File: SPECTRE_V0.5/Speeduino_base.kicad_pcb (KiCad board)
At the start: 2 copper layers, 100 x 93 mm, 213 parts, among them J1 Conn_01x06_Male, J2 Conn_02x04_Odd_Even, Q1 AO3400, Q10 AO3401A, Q11 AO3401A, Q12 BSP78, Q13 BSP78, Q14 BSP78, Q15 BSP78, Q16 AO3422, Q17 AO3422, Q18 BSP78, Q19 BSP78, Q2 AO3400, Q20 BSP78, Q21 AO3401A, Q22 AO3401A, Q23 BSP78, Q24 BSP78, Q25 BSP78, Q26 BSP78, Q3 AO3400, Q4 AO3400, Q5 AO3400, Q6 AO3400, Q7 AO3400, Q8 AO3422, Q9 AO3422, U1 MAX9926UAEE+, U2 LM78M05_TO220, U3 TL431DBZ, U4 molex_48pin, U5 TJA1050, U6 MAX3232

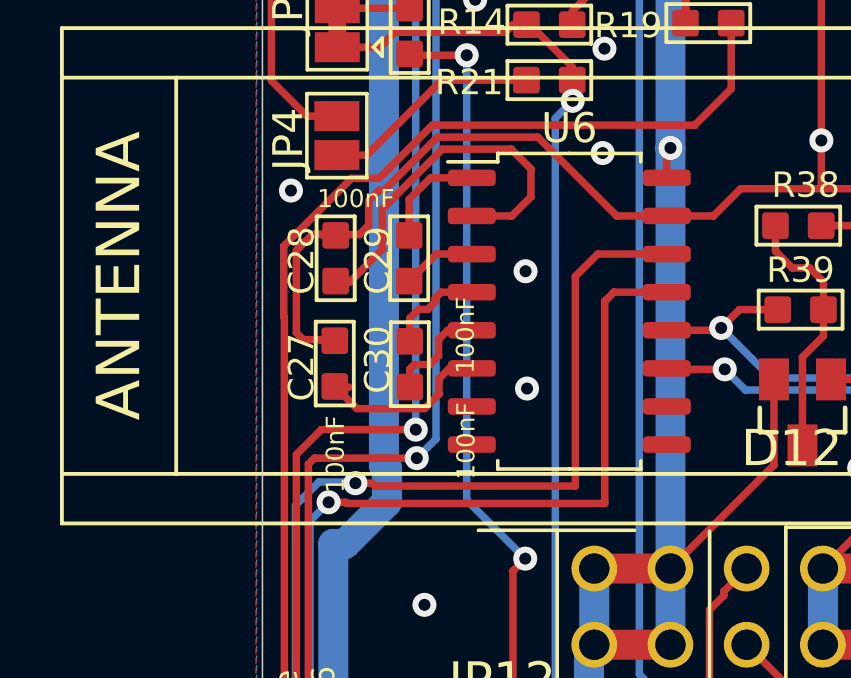
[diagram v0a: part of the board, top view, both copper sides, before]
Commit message: Removed peak&hold driver from this repo. Update resistor values in schematic to values that work. Cleaned up resistor naming.
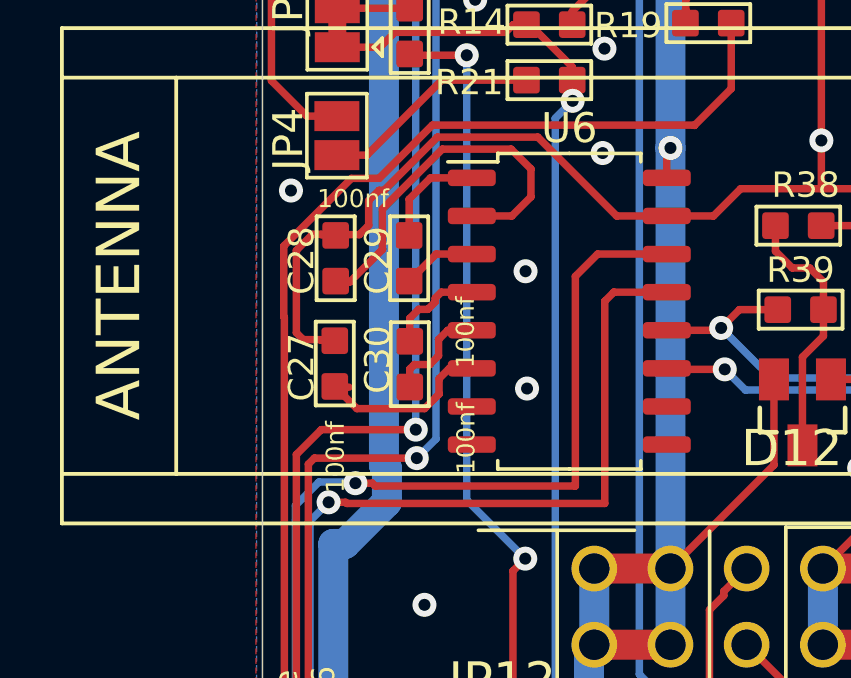
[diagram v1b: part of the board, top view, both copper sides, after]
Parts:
- C27, C28, C29, C30: value 100nF -> 100nf
- R10, R26, R29, R47: value 9.1k -> 9k1
- R25: value 4.7k -> 4K7
- R28, R46, R9: value 4.7k -> 4k7
- R34, R41, R52, R55, R61, R65, R84, R85, R88: value 100 -> 100R
- R44: value 8k3 -> 33k
- R45: value 1k2 -> 5k1
- R66: value 100k -> 10k
- R67: value 1k -> 100R
- R70: value 180 -> 220R
- R71: value 82 -> 100R
- R72: value 560 -> 470R
- R75: value 120 -> 120R
- R78, R79, R96, R97: value 470 -> 470R

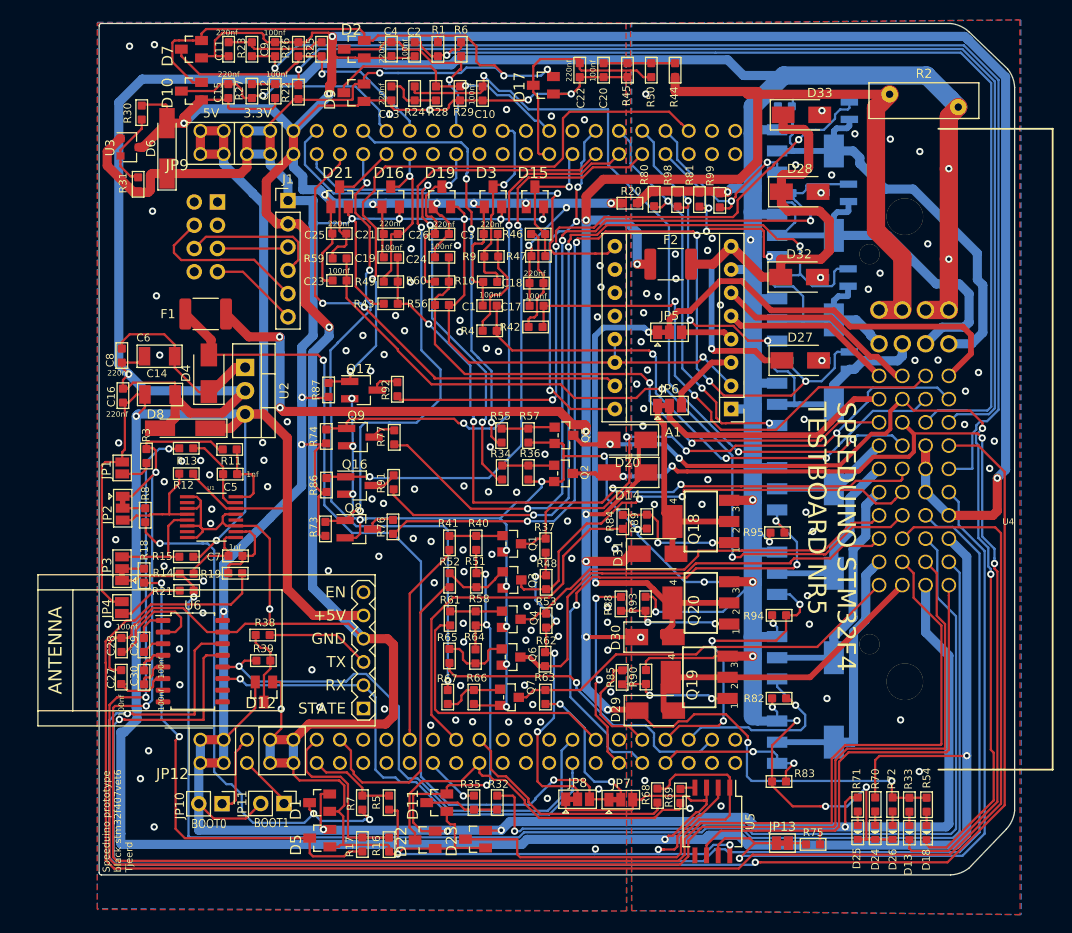
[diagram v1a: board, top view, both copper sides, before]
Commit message: clean-up board V0.5 started on board V0.5.1
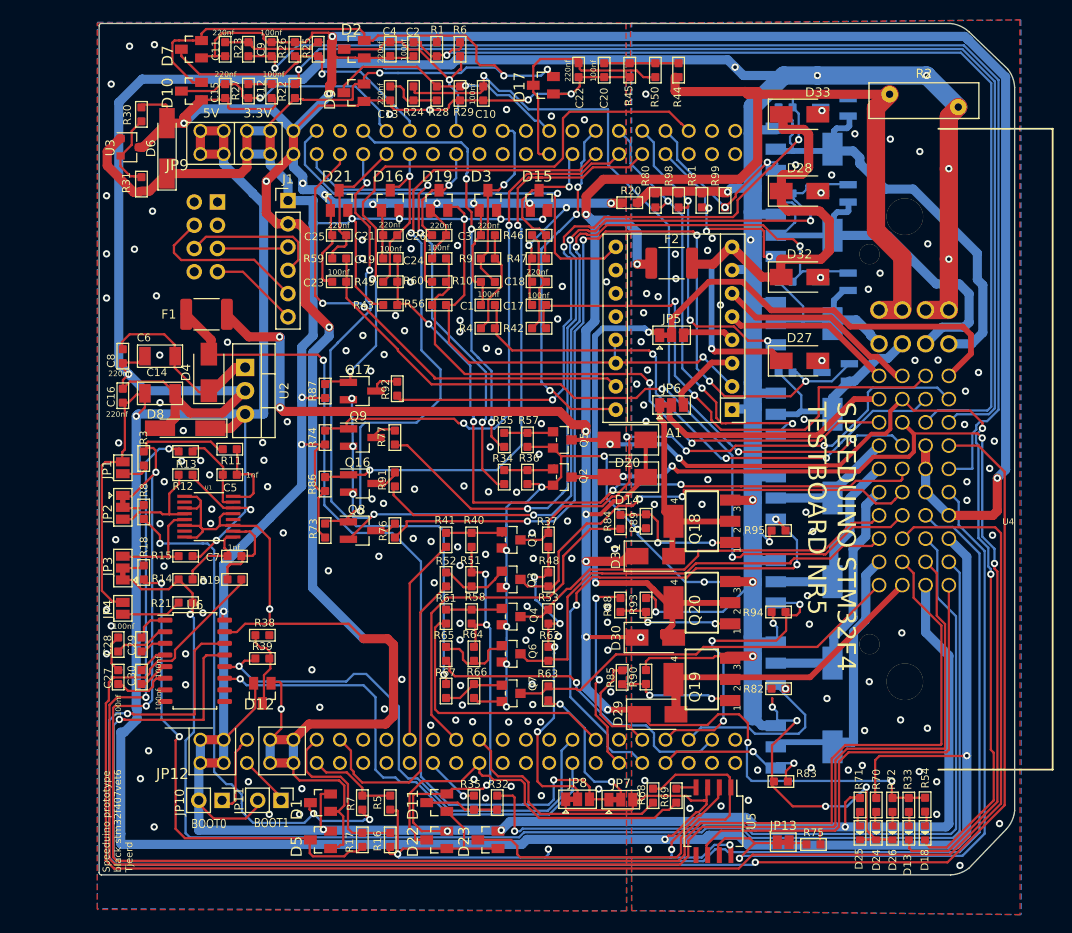
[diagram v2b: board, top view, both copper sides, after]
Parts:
- removed U$1: WIRELESS-BLUETOOTH-HC-05, Speeduino_base:WIRELESS-BLUETOOTH-HC-05
- moved D23 1.36 mm to (156.5, 106.2)
- moved R78 1.34 mm to (189.0, 55.1)
- moved R21 1.32 mm to (123.4, 80.3)
- moved Q10 1.29 mm to (194.4, 55.1)
- moved D22 1.27 mm to (150.9, 106.2)
- moved Q12 1.10 mm to (191.0, 59.7)
- moved R82 1.05 mm to (188.2, 89.7)
- moved Q24 1.02 mm to (191.0, 68.8)
- moved Q23 0.94 mm to (191.0, 78.0)
- moved R97 0.91 mm to (189.0, 45.2)
- moved R37 0.70 mm to (163.1, 73.4)
- moved R62 0.69 mm to (163.1, 85.9)
- moved D3 0.68 mm to (156.5, 36.3)
- moved R67 0.68 mm to (151.9, 89.9)
- moved R19 0.68 mm to (128.8, 77.7)
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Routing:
- net 5V: track 366.8 -> 331.9 mm, vias 4 -> 5
- net GND: track 631.2 -> 612.0 mm, vias 114 -> 141
- net /BT_TX: track 11.5 -> 0.00 mm
- net Net-(C28-Pad1): track 12.6 -> 6.03 mm
- net Net-(Q22-Pad1): track 83.0 -> 78.2 mm
- net PE9: track 44.6 -> 48.5 mm
- net VR2-: track 185.4 -> 181.9 mm
- net INJ6-OUT: track 25.1 -> 21.7 mm
- net Net-(Q10-Pad1): track 102.7 -> 99.4 mm
- net 3.3V: track 508.0 -> 504.8 mm
- net Net-(Q21-Pad1): track 88.4 -> 86.1 mm
- net VBAT_F1: track 96.1 -> 98.1 mm
- net PE13: track 21.8 -> 20.0 mm
- net BARO: track 57.8 -> 59.7 mm
- net PWR_GND: track 488.4 -> 490.2 mm, vias 71 -> 91
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
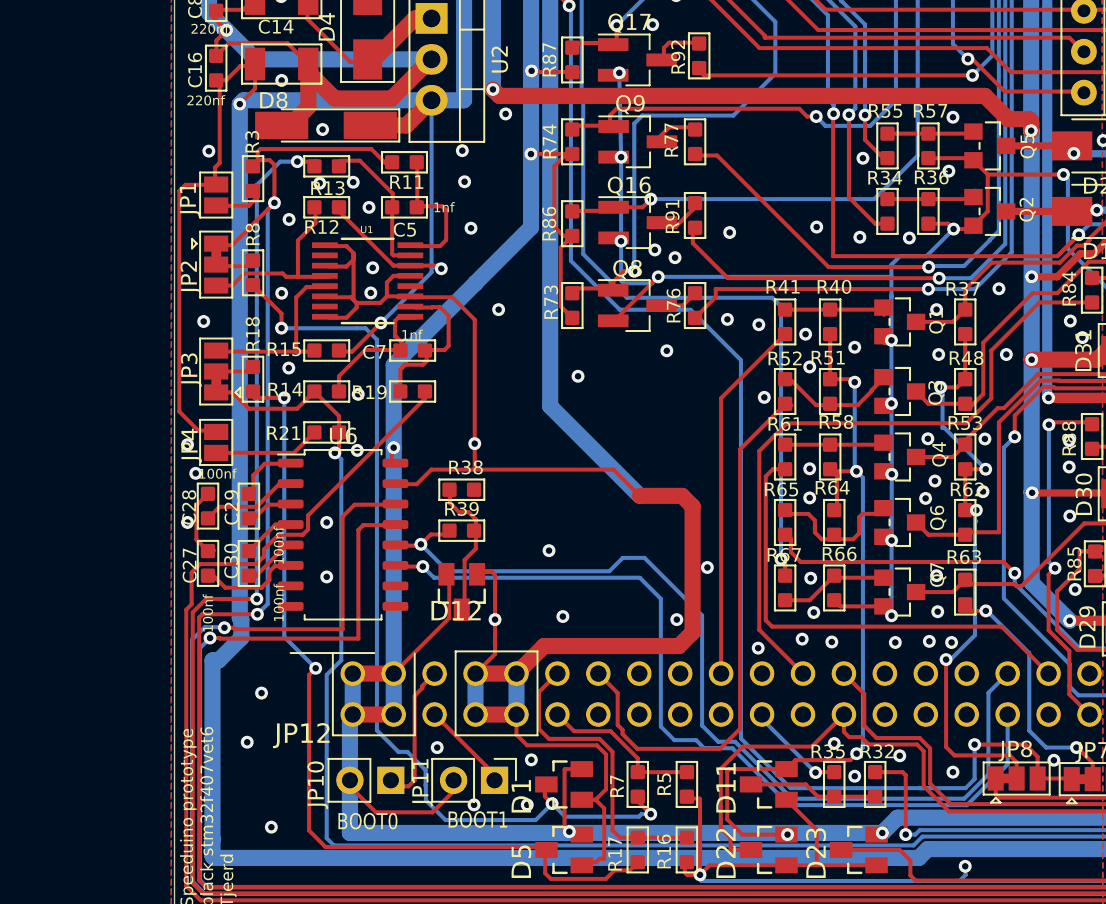
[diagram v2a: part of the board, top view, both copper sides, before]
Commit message: re-add bluetooth module
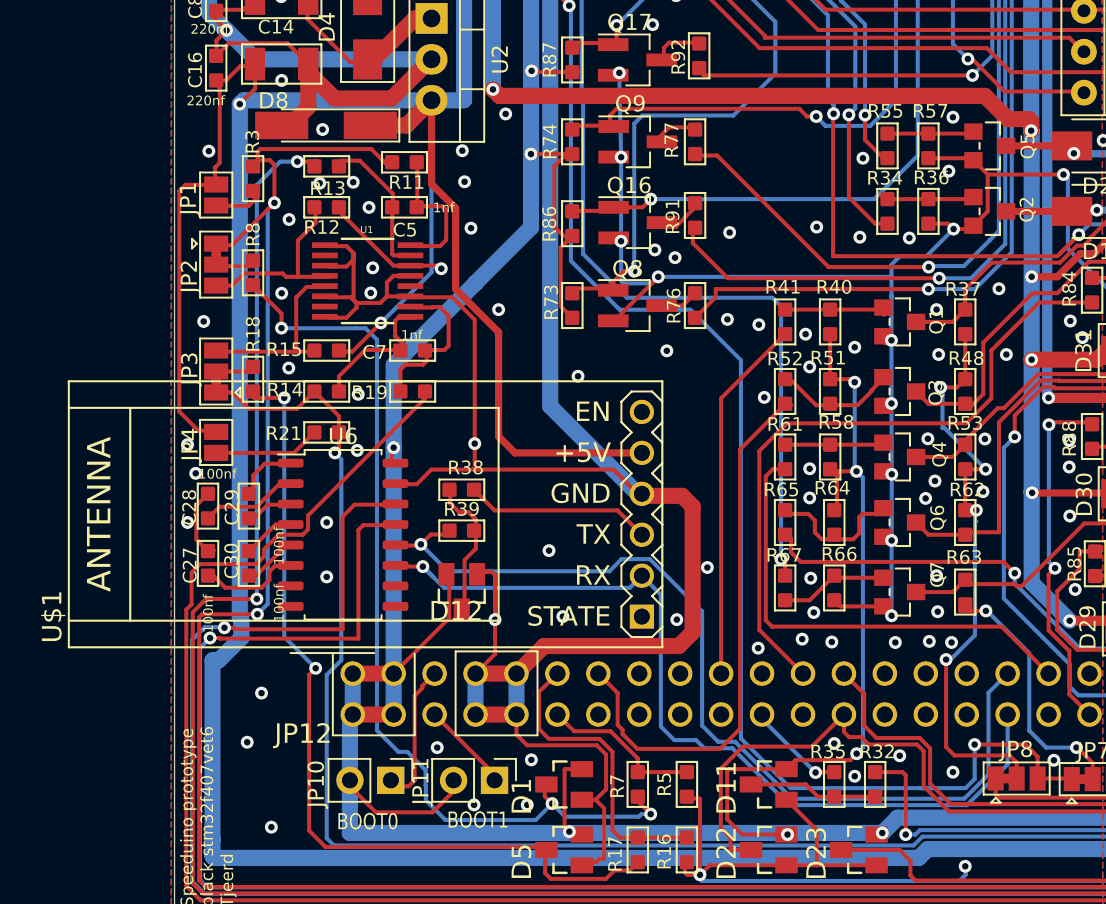
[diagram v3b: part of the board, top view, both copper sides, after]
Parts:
- added U$1: WIRELESS-BLUETOOTH-HC-05, Speeduino_base:WIRELESS-BLUETOOTH-HC-05, F.Cu at (125.9, 85.3)
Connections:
- net CLT_2 renamed AIN_3
- net IAT_2 renamed AIN_1
- net O2_2 renamed AIN_2
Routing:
- net 5V: track 331.9 -> 363.8 mm
- net /BT_TX: track 0.00 -> 11.6 mm
- net PA9: track 53.2 -> 54.9 mm
